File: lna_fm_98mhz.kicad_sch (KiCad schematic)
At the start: 26 parts, among them J1 SMA_50R_IN, J2 SMA_50R_OUT_BIAS, J3 BATTERY_PADS, Q1 MMBT5179

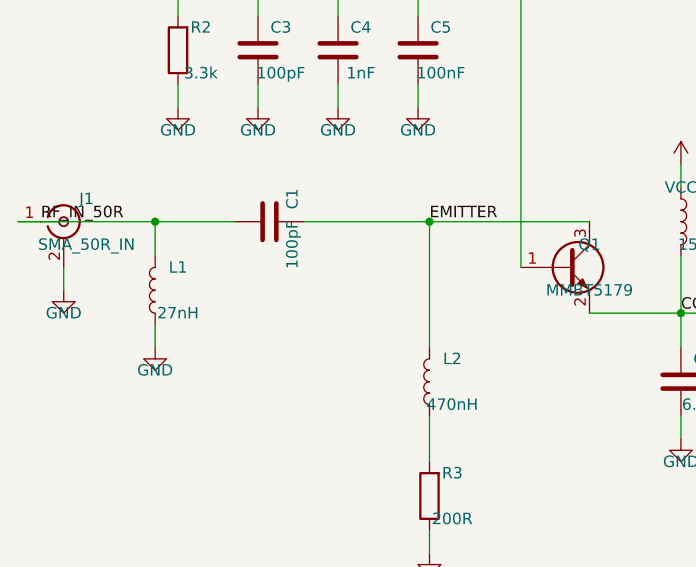
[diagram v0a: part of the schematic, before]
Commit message: Implement input bandpass pre-filter merged with input matching network
- Merged parallel LC tank (L1=18nH || C2=47pF) at 50-ohm RF input with series C1=100pF DC block to emitter.
- Suppresses out-of-band signals (<88 MHz shunted by L1, >108 MHz shunted by C2) while providing exact step-down transformation to low-impedance common-base emitter.
- Preserves 98 MHz center performance: S21 = +19.88 dB, S11 = -22.27 dB (VSWR 1.17:1), Zin = 43.1 - j1.9 Ohm.
- Updated Qucs simulation netlists, Touchstone s2p, and schematic generator scripts.
- Updated KiCad schematic, zero ERC violations.
- Synthesized PCB layout with C2 placed and routed, zero DRC errors.
- Regenerated production Gerbers, Excellon drill files, 3D STEP model, and 2D/3D visual renders.
- Updated README.md and AGENT.md documentation and BOM.
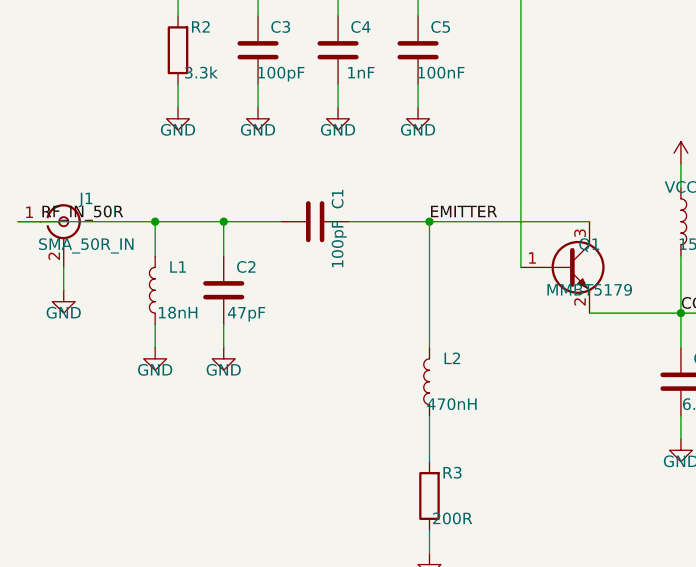
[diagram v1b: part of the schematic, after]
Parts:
- added C2: 47pF, Capacitor_SMD:C_0603_1608Metric, symbol Device:C
- L1: value 27nH -> 18nH
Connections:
- net GND: now also C2.1
- net RF_IN_50R: now also C2.2

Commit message: Optimize input matching network for -31.87 dB return loss at 98 MHz
- Parameter optimization: L1=22nH (0603 E12), C2=27pF (0603 E12), C1=91pF (0805 E24).
- Restores real input resistance to 52.5 Ohm (from 43.1 Ohm) by tuning C1 transformation Q.
- Improves S11 return loss from -22.27 dB to -31.87 dB (VSWR 1.05:1).
- Preserves high gain (S21 = +19.91 dB) and out-of-band rejection (-19.9 dB at 50 MHz, +2.1 dB at 200 MHz).
- Updated Qucs netlists, Touchstone s2p, and schematic generators.
- Regenerated KiCad schematic and PCB layout with 0 ERC / 0 DRC violations.
- Regenerated production Gerbers, Excellon drills, 3D STEP model, and 2D/3D renders.
- Updated README.md, AGENT.md, and PRE_FILTER_COMPARISON.md.
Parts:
- C1: value 100pF -> 91pF
- C2: value 47pF -> 27pF
- L1: value 18nH -> 22nH
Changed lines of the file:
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@@
 			)
 		)
-		(property "Value" "18nH"
+		(property "Value" "22nH"
 			(at 48.26 71.12 0)
 			(effects
@@
 			)
 		)
-		(property "Value" "47pF"
+		(property "Value" "27pF"
 			(at 55.88 71.12 0)
 			(effects
@@
 			)
 		)
-		(property "Value" "100pF"
+		(property "Value" "91pF"
 			(at 66.04 63.50 0)
 			(effects
